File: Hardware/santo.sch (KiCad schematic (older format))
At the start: 1 part

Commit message: partial need to finish wiring up usb-c
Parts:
- added C1: 10uF, symbol C
- added C2: 1uF, symbol C
- added J?: USB_C_Receptacle, symbol USB_C_Receptacle
- added R1, R2: 22k, symbol R_Small
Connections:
- net at U?.14 (VCC): now also U?.15 (GND), U?.2 (UVCC), U?.23 (GND), U?.24 (AVCC), U?.34 (VCC), U?.35 (GND), U?.43 (GND), U?.44 (AVCC), C2.2, J?.A1 (GND), J?.A12 (GND), J?.B1 (GND), J?.B12 (GND)
- net at U?.3 (D-): now also R1.2
- net at U?.4 (D+): now also R2.2
- net at U?.6 (UCAP): now also C2.1
- net at U?.7 (VBUS): now also C1.2
- new net: C1.1, J?.A4 (VBUS), J?.A9 (VBUS), J?.B4 (VBUS), J?.B9 (VBUS)
- new net: J?.A6 (D+), J?.B6 (D+), R2.1
- new net: J?.A7 (D-), J?.B7 (D-), R1.1
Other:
- moved on the sheet: U?
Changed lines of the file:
@@
 LIBS:contrib
 LIBS:valves
+LIBS:santo-cache
 EELAYER 25 0
 EELAYER END
@@
 L ATMEGA32U4-AU U?
 U 1 1 59F3E9EC
-P 5900 3450
-F 0 "U?" H 4950 5150 50  0000 C CNN
-F 1 "ATMEGA32U4-AU" H 6600 1950 50  0000 C CNN
-F 2 "TQFP44" H 5900 3450 50  0001 C CIN
-F 3 "" H 7000 4550 50  0001 C CNN
-	1    5900 3450
+P 5800 4350
+F 0 "U?" H 4850 6050 50  0000 C CNN
+F 1 "ATMEGA32U4-AU" H 6500 2850 50  0000 C CNN
+F 2 "TQFP44" H 5800 4350 50  0001 C CIN
+F 3 "" H 6900 5450 50  0001 C CNN
+	1    5800 4350
 	1    0    0    -1
 $EndComp
+$Comp
+L USB_C_Receptacle J?
+U 1 1 59F5288B
+P 1000 4150
+F 0 "J?" H 600 5600 50  0000 L CNN
+F 1 "USB_C_Receptacle" H 1400 5600 50  0000 R CNN
+F 2 "" H 1150 4150 50  0001 C CNN
+F 3 "" H 1150 4150 50  0001 C CNN
+	1    1000 4150
+	1    0    0    -1
+$EndComp
+Wire Wire Line
+	1600 2950 1800 2950
+Wire Wire Line
+	1800 2850 1800 3150
+Connection ~ 1800 2850
+Wire Wire Line
+	1800 3050 1600 3050
+Connection ~ 1800 2950
+Wire Wire Line
+	1800 3150 1600 3150
+Connection ~ 1800 3050
+$Comp
+L R_Small R2
+U 1 1 59F52DAB
+P 3100 4350
+F 0 "R2" H 3130 4370 50  0000 L CNN
+F 1 "22k" H 3130 4310 50  0000 L CNN
+F 2 "" H 3100 4350 50  0001 C CNN
+F 3 "" H 3100 4350 50  0001 C CNN
+	1    3100 4350
+	1    0    0    -1
+$EndComp
+$Comp
+L R_Small R1
+U 1 1 59F52DD6
+P 3100 4050
+F 0 "R1" H 3130 4070 50  0000 L CNN
+F 1 "22k" H 3130 4010 50  0000 L CNN
+F 2 "" H 3100 4050 50  0001 C CNN
+F 3 "" H 3100 4050 50  0001 C CNN
+	1    3100 4050
+	1    0    0    -1
+$EndComp
+Wire Wire Line
+	1600 3650 3100 3650
+Wire Wire Line
+	3100 3650 3100 3950
+Wire Wire Line
+	1600 3750 3100 3750
+Connection ~ 3100 3750
+Wire Wire Line
+	3100 4150 4250 4150
+Wire Wire Line
+	4250 4150 4250 4250
+Wire Wire Line
+	4250 4250 4650 4250
+Wire Wire Line
+	1600 3850 2950 3850
+Wire Wire Line
+	2950 3850 2950 4250
+Wire Wire Line
+	2950 4250 3100 4250
+Wire Wire Line
+	1600 3950 2950 3950
+Connection ~ 2950 3950
+Wire Wire Line
+	3100 4450 3800 4450
+Wire Wire Line
+	3800 4450 3800 4100
+Wire Wire Line
+	3800 4100 4600 4100
+Wire Wire Line
+	4600 4100 4600 4150
+Wire Wire Line
+	4600 4150 4650 4150
+Wire Wire Line
+	1600 2850 2850 2850
+$Comp
+L C C1
+U 1 1 59F5311D
+P 2850 3000
+F 0 "C1" H 2875 3100 50  0000 L CNN
+F 1 "10uF" H 2875 2900 50  0000 L CNN
+F 2 "" H 2888 2850 50  0001 C CNN
+F 3 "" H 2850 3000 50  0001 C CNN
+	1    2850 3000
+	1    0    0    -1
+$EndComp
+Wire Wire Line
+	2850 3150 3800 3150
+Wire Wire Line
+	3800 3150 3800 4000
+Wire Wire Line
+	3800 4000 4650 4000
+$Comp
+L C C2
+U 1 1 59F532C4
+P 4350 4550
+F 0 "C2" H 4375 4650 50  0000 L CNN
+F 1 "1uF" H 4375 4450 50  0000 L CNN
+F 2 "" H 4388 4400 50  0001 C CNN
+F 3 "" H 4350 4550 50  0001 C CNN
+	1    4350 4550
+	1    0    0    -1
+$EndComp
+Wire Wire Line
+	4350 4400 4650 4400
+Wire Wire Line
+	4350 4700 4350 5950
+Wire Wire Line
+	4350 5950 800  5950
+Wire Wire Line
+	800  5950 800  5750
+Wire Wire Line
+	900  5750 900  5950
+Connection ~ 900  5950
+Wire Wire Line
+	1000 5750 1000 5950
+Connection ~ 1000 5950
+Wire Wire Line
+	1100 5750 1100 5950
+Connection ~ 1100 5950
+Wire Wire Line
+	5350 2550 5350 2300
+Wire Wire Line
+	5350 2300 7300 2300
+Wire Wire Line
+	7300 2300 7300 6300
+Wire Wire Line
+	7300 6300 2750 6300
+Wire Wire Line
+	2750 6300 2750 5950
+Connection ~ 2750 5950
+Wire Wire Line
+	5600 2550 5600 2300
+Connection ~ 5600 2300
+Wire Wire Line
+	5700 2550 5700 2300
+Connection ~ 5700 2300
+Wire Wire Line
+	5950 2550 5950 2300
+Connection ~ 5950 2300
+Wire Wire Line
+	6050 2550 6050 2300
+Connection ~ 6050 2300
+Wire Wire Line
+	5650 5950 5650 6300
+Connection ~ 5650 6300
+Wire Wire Line
+	5750 5950 5750 6300
+Connection ~ 5750 6300
+Wire Wire Line
+	5850 5950 5850 6300
+Connection ~ 5850 6300
+Wire Wire Line
+	5950 5950 5950 6300
+Connection ~ 5950 6300
 $EndSCHEMATC

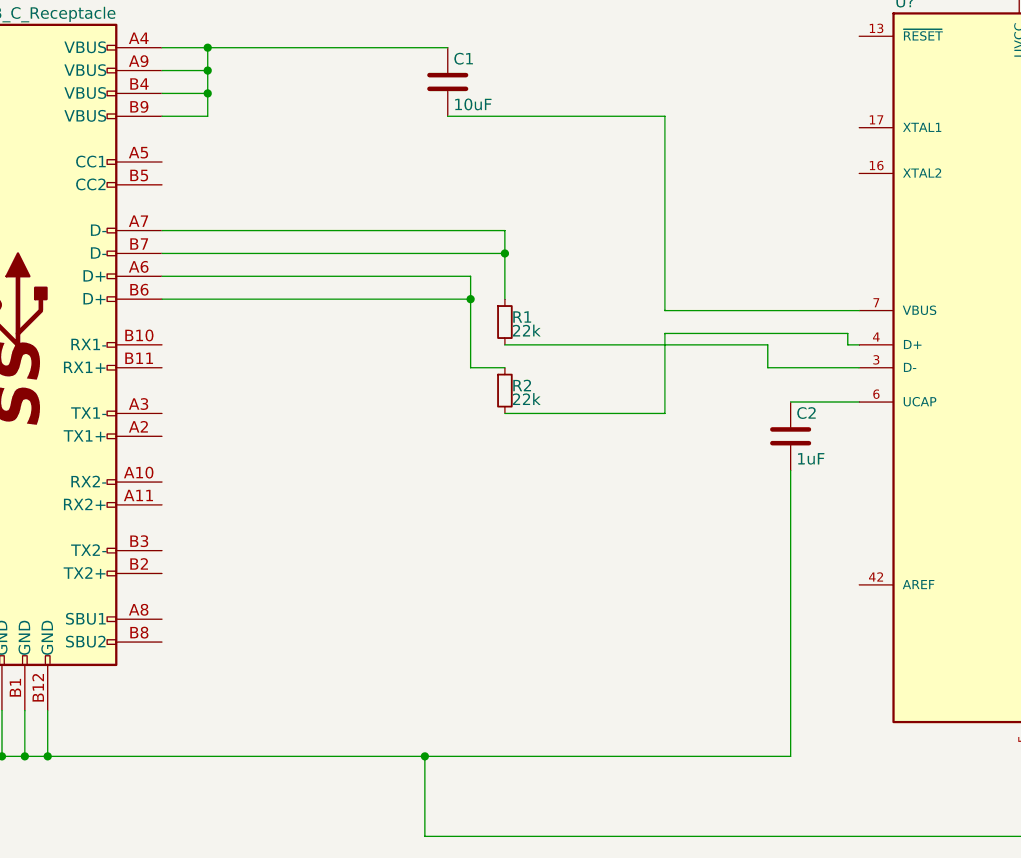
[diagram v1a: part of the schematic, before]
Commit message: Finish up wiring in the USB-C Receptacle
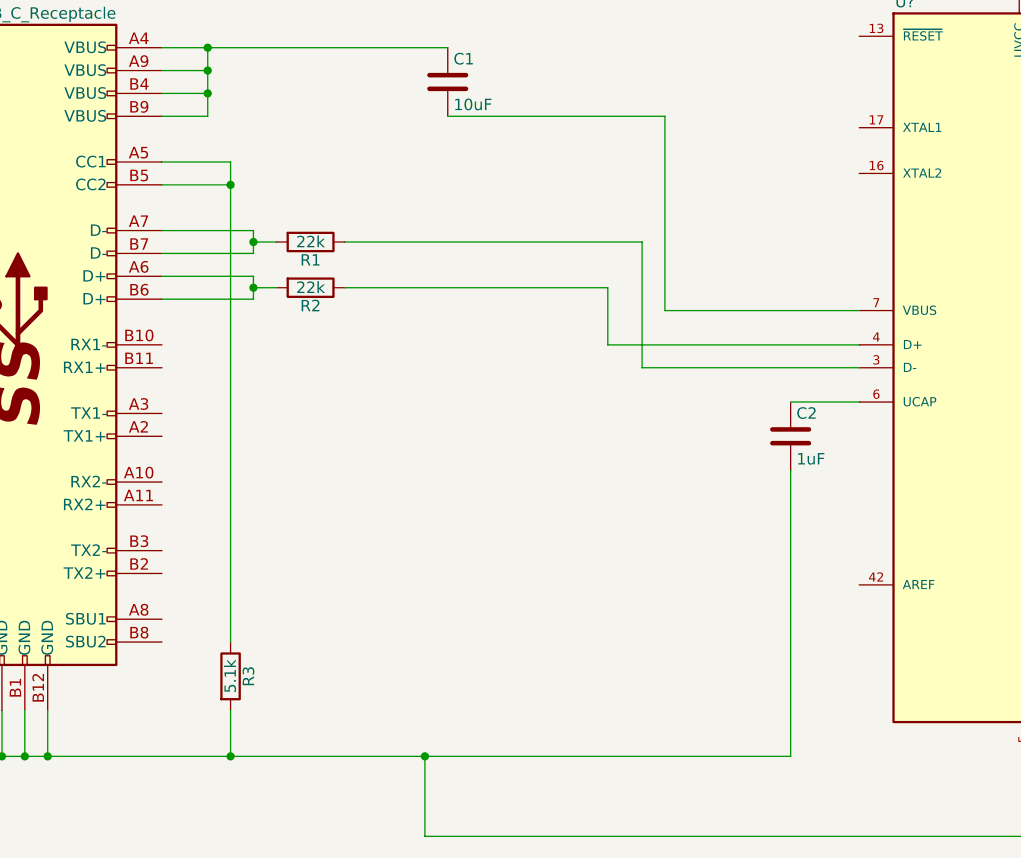
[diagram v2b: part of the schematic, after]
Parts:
- removed R1, R2: 22k, symbol R_Small
- added R1, R2: 22k, symbol R
- added R3: 5.1k, symbol R
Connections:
- net at C2.2, J?.A1 (GND), J?.A12 (GND)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: now also R3.2
- net at U?.3 (D-): now also R1.1
- net at U?.4 (D+): now also R2.1
- net at J?.A5 (CC1): now also J?.B5 (CC2), R3.1
- net at J?.A6 (D+), J?.B6 (D+): now also R2.2
- net at J?.A7 (D-), J?.B7 (D-): now also R1.2
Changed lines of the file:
@@
 	1800 3150 1600 3150
 Connection ~ 1800 3050
-$Comp
-L R_Small R2
-U 1 1 59F52DAB
-P 3100 4350
-F 0 "R2" H 3130 4370 50  0000 L CNN
-F 1 "22k" H 3130 4310 50  0000 L CNN
-F 2 "" H 3100 4350 50  0001 C CNN
-F 3 "" H 3100 4350 50  0001 C CNN
-	1    3100 4350
-	1    0    0    -1
-$EndComp
-$Comp
-L R_Small R1
-U 1 1 59F52DD6
-P 3100 4050
-F 0 "R1" H 3130 4070 50  0000 L CNN
-F 1 "22k" H 3130 4010 50  0000 L CNN
-F 2 "" H 3100 4050 50  0001 C CNN
-F 3 "" H 3100 4050 50  0001 C CNN
-	1    3100 4050
-	1    0    0    -1
-$EndComp
-Wire Wire Line
-	1600 3650 3100 3650
-Wire Wire Line
-	3100 3650 3100 3950
-Wire Wire Line
-	1600 3750 3100 3750
-Connection ~ 3100 3750
-Wire Wire Line
-	3100 4150 4250 4150
-Wire Wire Line
-	4250 4150 4250 4250
-Wire Wire Line
-	4250 4250 4650 4250
-Wire Wire Line
-	1600 3850 2950 3850
-Wire Wire Line
-	2950 3850 2950 4250
-Wire Wire Line
-	2950 4250 3100 4250
-Wire Wire Line
-	1600 3950 2950 3950
-Connection ~ 2950 3950
-Wire Wire Line
-	3100 4450 3800 4450
-Wire Wire Line
-	3800 4450 3800 4100
-Wire Wire Line
-	3800 4100 4600 4100
-Wire Wire Line
-	4600 4100 4600 4150
-Wire Wire Line
-	4600 4150 4650 4150
 Wire Wire Line
 	1600 2850 2850 2850
@@
 	5950 5950 5950 6300
 Connection ~ 5950 6300
+$Comp
+L R R3
+U 1 1 59F605C4
+P 1900 5600
+F 0 "R3" V 1980 5600 50  0000 C CNN
+F 1 "5.1k" V 1900 5600 50  0000 C CNN
+F 2 "" V 1830 5600 50  0001 C CNN
+F 3 "" H 1900 5600 50  0001 C CNN
+	1    1900 5600
+	1    0    0    -1
+$EndComp
+Wire Wire Line
+	1600 3350 1900 3350
+Wire Wire Line
+	1900 3350 1900 5450
+Wire Wire Line
+	1600 3450 1900 3450
+Connection ~ 1900 3450
+Wire Wire Line
+	1900 5750 1900 5950
+Connection ~ 1900 5950
+$Comp
+L R R1
+U 1 1 59F60892
+P 2250 3700
+F 0 "R1" V 2330 3700 50  0000 C CNN
+F 1 "22k" V 2250 3700 50  0000 C CNN
+F 2 "" V 2180 3700 50  0001 C CNN
+F 3 "" H 2250 3700 50  0001 C CNN
+	1    2250 3700
+	0    1    1    0
+$EndComp
+$Comp
+L R R2
+U 1 1 59F608F2
+P 2250 3900
+F 0 "R2" V 2330 3900 50  0000 C CNN
+F 1 "22k" V 2250 3900 50  0000 C CNN
+F 2 "" V 2180 3900 50  0001 C CNN
+F 3 "" H 2250 3900 50  0001 C CNN
+	1    2250 3900
+	0    1    1    0
+$EndComp
+Wire Wire Line
+	1600 3650 2000 3650
+Wire Wire Line
+	2000 3650 2000 3750
+Wire Wire Line
+	2000 3700 2100 3700
+Wire Wire Line
+	2000 3750 1600 3750
+Connection ~ 2000 3700
+Wire Wire Line
+	2000 3950 1600 3950
+Wire Wire Line
+	2000 3850 2000 3950
+Wire Wire Line
+	2000 3900 2100 3900
+Wire Wire Line
+	1600 3850 2000 3850
+Connection ~ 2000 3900
+Wire Wire Line
+	2400 3700 3700 3700
+Wire Wire Line
+	3700 3700 3700 4250
+Wire Wire Line
+	3700 4250 4650 4250
+Wire Wire Line
+	2400 3900 3550 3900
+Wire Wire Line
+	3550 3900 3550 4150
+Wire Wire Line
+	3550 4150 4650 4150
 $EndSCHEMATC
